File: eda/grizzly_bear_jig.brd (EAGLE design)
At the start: 76.2 x 69.8 mm, 28 parts, among them U1 ISL83491SOIC

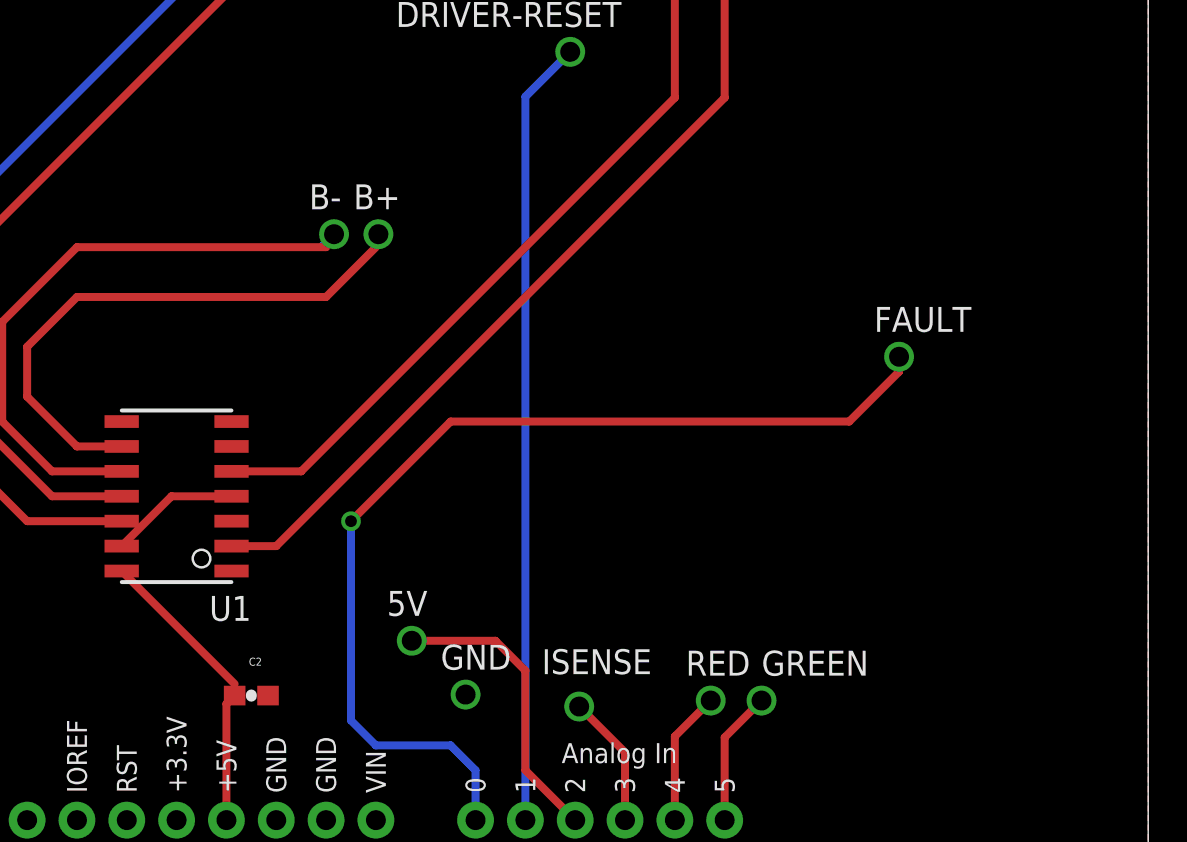
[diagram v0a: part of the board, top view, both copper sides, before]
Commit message: Changed some version numbers,  made hot fixes on grizzly jig.
Changed & updated Smartsensor, Grizzly Jig, Koala
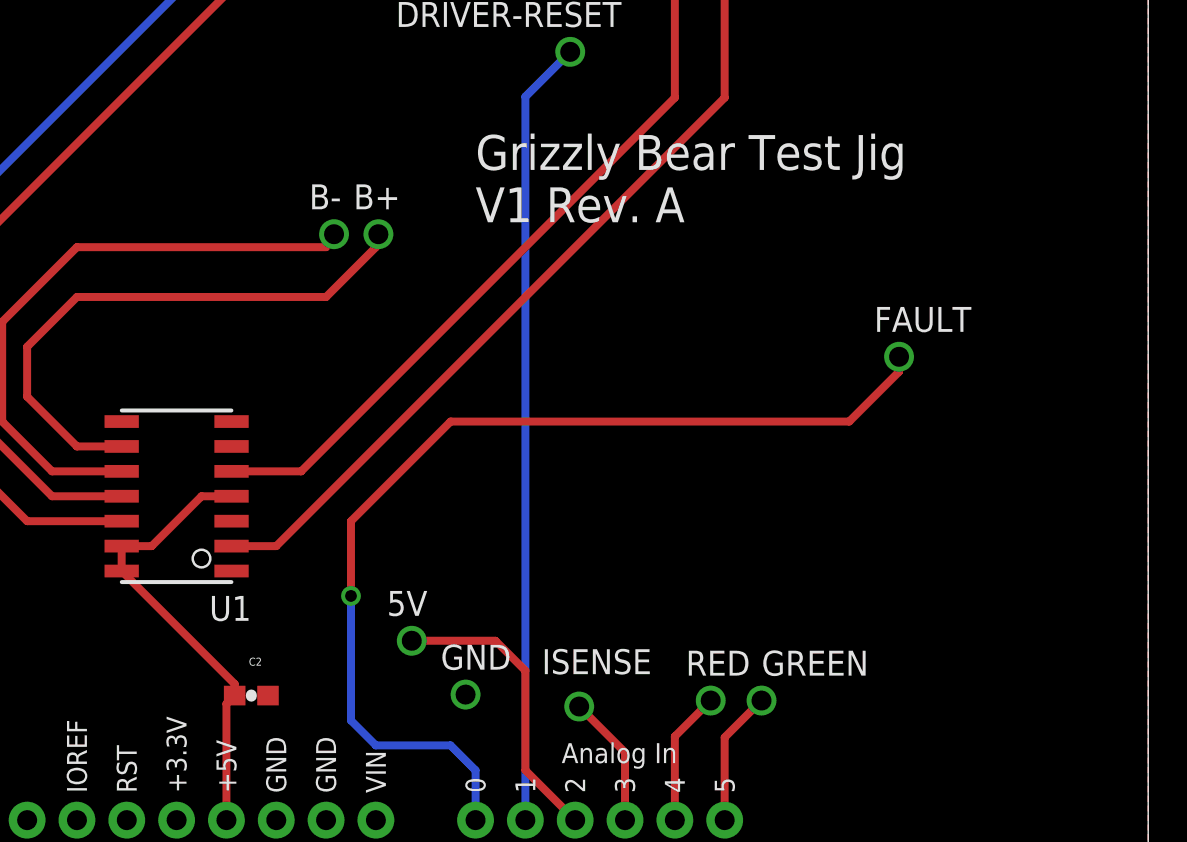
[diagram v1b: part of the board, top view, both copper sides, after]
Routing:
- net 5V: track 21.3 -> 23.4 mm
- net B-: track 32.1 -> 31.1 mm
- net B+: track 28.3 -> 29.1 mm
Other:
- board text added: "(c) Pioneers in Engineering. Design by: Tony Abdo and Andrew Wang. This design is open source hardware. For more information, visit pioneers.berkeley.edu/opensource."
- board text added: "Grizzly Bear Test Jig V1 Rev. A"
